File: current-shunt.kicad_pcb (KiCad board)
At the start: 4 copper layers, 130 x 50 mm, 187 parts, among them J1 Screw_Terminal_01x03, J2 Screw_Terminal_01x03, J3 Screw_Terminal_01x03, J4 Conn_01x02, J5 Conn_01x04, J6 Conn_01x04, U1 ADS1015IDGS, U2 INA219AxD, U3 INA219AxD, U4 INA219AxD, U5 MCP9804_MSOP, U6 M24C02-WMN, U7 TSR_1-2450, U8 ISO1541, U9 SRV05-4

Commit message: Add labels to board and update not available component
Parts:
- D15, D16, D19, D26, D27, D30, D35, D4, D5, D8: value P4SMAJ20CA -> SMAJ20CA
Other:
- board text added: "https://github.com/tdittr/tripple-current-shunt ${DATE} ${REV} CERN-OHL-P-2.0"
- board text removed: "https://github.com/tdittr/tripple-current-shunt CERN-OHL-P-2.0"
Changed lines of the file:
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@@
     )
   )
+  (property "DATE" "2022-10-28")
+  (property "REV" "rev1")
   (net 0 "")
   (net 1 "/shunt-a/IN+")
@@
     (descr "Diode SMA (DO-214AC)")
     (tags "Diode SMA (DO-214AC)")
-    (property "LCSC Part #" "C391567")
+    (property "LCSC Part #" "C309871")
     (property "Sheetfile" "File: shunt.kicad_sch")
     (property "Sheetname" "shunt-b")
@@
       (effects (font (size 1 1) (thickness 0.15)))
     )
-    (fp_text value "P4SMAJ20CA" (at 0 2.6 90) (layer "F.Fab")
+    (fp_text value "SMAJ20CA" (at 0 2.6 90) (layer "F.Fab")
       (effects (font (size 1 1) (thickness 0.15)))
     )
@@
     (descr "Diode SMA (DO-214AC)")
     (tags "Diode SMA (DO-214AC)")
-    (property "LCSC Part #" "C391567")
+    (property "LCSC Part #" "C309871")
     (property "Sheetfile" "File: shunt.kicad_sch")
     (property "Sheetname" "shunt-c")
@@
       (effects (font (size 1 1) (thickness 0.15)))
     )
-    (fp_text value "P4SMAJ20CA" (at 0 2.6 90) (layer "F.Fab")
+    (fp_text value "SMAJ20CA" (at 0 2.6 90) (layer "F.Fab")
       (effects (font (size 1 1) (thickness 0.15)))
     )
@@
     (descr "Diode SMA (DO-214AC)")
     (tags "Diode SMA (DO-214AC)")
-    (property "LCSC Part #" "C391567")
+    (property "LCSC Part #" "C309871")
     (property "Sheetfile" "File: shunt.kicad_sch")
     (property "Sheetname" "shunt-c")
@@
       (effects (font (size 1 1) (thickness 0.15)))
     )
-    (fp_text value "P4SMAJ20CA" (at 0 2.6 90) (layer "F.Fab")
+    (fp_text value "SMAJ20CA" (at 0 2.6 90) (layer "F.Fab")
       (effects (font (size 1 1) (thickness 0.15)))
     )
@@
     (descr "Diode SMA (DO-214AC)")
     (tags "Diode SMA (DO-214AC)")
-    (property "LCSC Part #" "C391567")
+    (property "LCSC Part #" "C309871")
     (property "Sheetfile" "File: shunt.kicad_sch")
     (property "Sheetname" "shunt-c")
@@
       (effects (font (size 1 1) (thickness 0.15)))
     )
-    (fp_text value "P4SMAJ20CA" (at 0 2.6 90) (layer "F.Fab")
+    (fp_text value "SMAJ20CA" (at 0 2.6 90) (layer "F.Fab")
       (effects (font (size 1 1) (thickness 0.15)))
     )
@@
     (descr "Diode SMA (DO-214AC)")
     (tags "Diode SMA (DO-214AC)")
-    (property "LCSC Part #" "C391567")
+    (property "LCSC Part #" "C309871")
     (property "Sheetfile" "File: shunt.kicad_sch")
     (property "Sheetname" "shunt-a")
@@
       (effects (font (size 1 1) (thickness 0.15)))
     )
-    (fp_text value "P4SMAJ20CA" (at 0 2.6 90) (layer "F.Fab")
+    (fp_text value "SMAJ20CA" (at 0 2.6 90) (layer "F.Fab")
       (effects (font (size 1 1) (thickness 0.15)))
     )
@@
     (descr "Diode SMA (DO-214AC)")
     (tags "Diode SMA (DO-214AC)")
-    (property "LCSC Part #" "C391567")
+    (property "LCSC Part #" "C309871")
     (property "Sheetfile" "File: shunt.kicad_sch")
     (property "Sheetname" "shunt-b")
@@
       (effects (font (size 1 1) (thickness 0.15)))
     )
-    (fp_text value "P4SMAJ20CA" (at 0 2.6 90) (layer "F.Fab")
+    (fp_text value "SMAJ20CA" (at 0 2.6 90) (layer "F.Fab")
       (effects (font (size 1 1) (thickness 0.15)))
     )
@@
     (descr "Diode SMA (DO-214AC)")
     (tags "Diode SMA (DO-214AC)")
-    (property "LCSC Part #" "C391567")
+    (property "LCSC Part #" "C309871")
     (property "Sheetfile" "File: shunt.kicad_sch")
     (property "Sheetname" "shunt-b")
@@
       (effects (font (size 1 1) (thickness 0.15)))
     )
-    (fp_text value "P4SMAJ20CA" (at 0 2.6 90) (layer "F.Fab")
+    (fp_text value "SMAJ20CA" (at 0 2.6 90) (layer "F.Fab")
       (effects (font (size 1 1) (thickness 0.15)))
     )
@@
     (descr "Diode SMA (DO-214AC)")
     (tags "Diode SMA (DO-214AC)")
-    (property "LCSC Part #" "C391567")
+    (property "LCSC Part #" "C309871")
     (property "Sheetfile" "File: shunt.kicad_sch")
     (property "Sheetname" "shunt-a")
@@
       (effects (font (size 1 1) (thickness 0.15)))
     )
-    (fp_text value "P4SMAJ20CA" (at 0 2.6 90) (layer "F.Fab")
+    (fp_text value "SMAJ20CA" (at 0 2.6 90) (layer "F.Fab")
       (effects (font (size 1 1) (thickness 0.15)))
     )
@@
     (descr "Diode SMA (DO-214AC)")
     (tags "Diode SMA (DO-214AC)")
-    (property "LCSC Part #" "C391567")
+    (property "LCSC Part #" "C309871")
     (property "Sheetfile" "File: shunt.kicad_sch")
     (property "Sheetname" "shunt-a")
@@
       (effects (font (size 1 1) (thickness 0.15)))
     )
-    (fp_text value "P4SMAJ20CA" (at 0 2.6 90) (layer "F.Fab")
+    (fp_text value "SMAJ20CA" (at 0 2.6 90) (layer "F.Fab")
       (effects (font (size 1 1) (thickness 0.15)))
     )
@@
     (descr "Diode SMA (DO-214AC)")
     (tags "Diode SMA (DO-214AC)")
-    (property "LCSC Part #" "C391567")
+    (property "LCSC Part #" "C309871")
     (property "Sheetfile" "File: current-shunt.kicad_sch")
     (property "Sheetname" "")
@@
       (effects (font (size 1 1) (thickness 0.15)))
     )
-    (fp_text value "P4SMAJ20CA" (at 0 2.6 90) (layer "F.Fab")
+    (fp_text value "SMAJ20CA" (at 0 2.6 90) (layer "F.Fab")
       (effects (font (size 1 1) (thickness 0.15)))
     )
@@
     (effects (font (size 1 1) (thickness 0.15)) (justify mirror))
   )
-  (gr_text "https://github.com/tdittr/tripple-current-shunt\nCERN-OHL-P-2.0" (at 154.305 60.325) (layer "B.SilkS")
-    (effects (font (size 1 1) (thickness 0.15)) (justify mirror))
+  (gr_text "https://github.com/tdittr/tripple-current-shunt\n${DATE} ${REV}\nCERN-OHL-P-2.0" (at 171.25 60.75) (layer "B.SilkS")
+    (effects (font (size 1 1) (thickness 0.15)) (justify left mirror))
   )
   (gr_text "I2C\nPullUp" (at 175.26 43.815) (layer "B.SilkS")

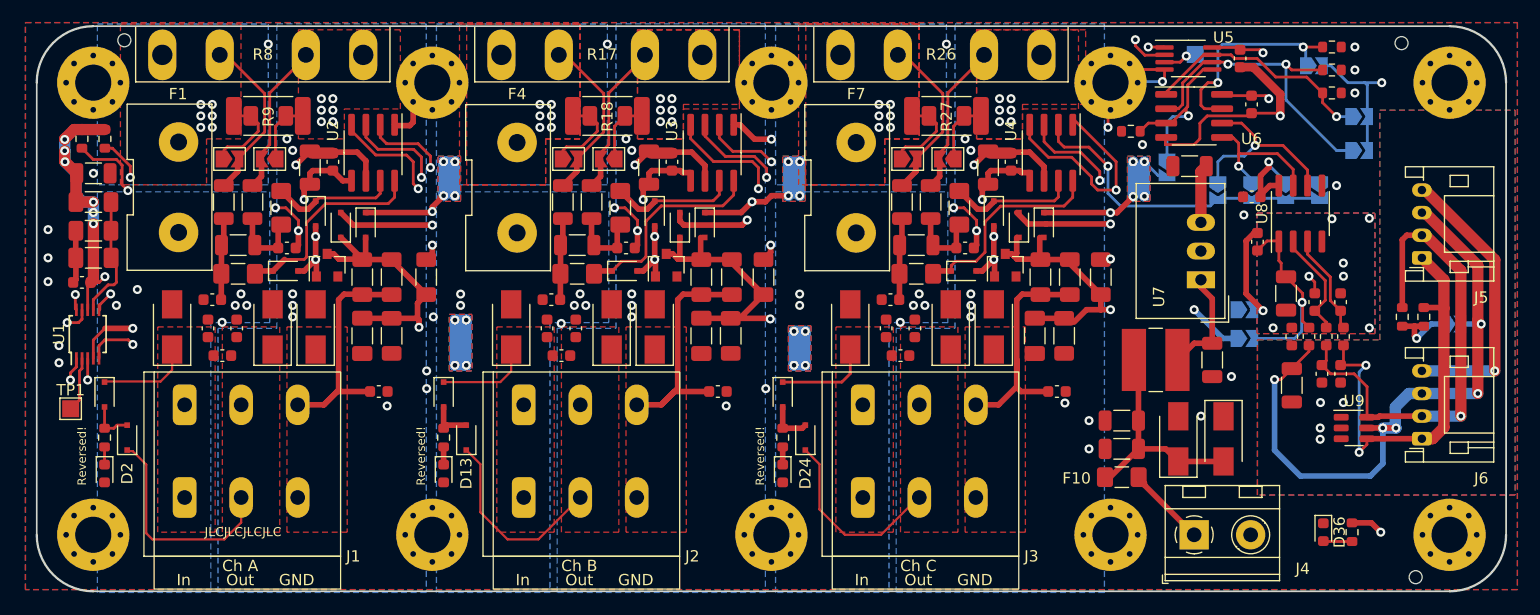
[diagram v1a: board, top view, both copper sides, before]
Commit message: Shrink board and reduce features to reduce price
* Shrink to 100mm x 50mm
* Remove voltage regulator and use Stemma Power instead
* Remove isolation (is easier to add outside when needed)
* Remove reverse indicators to save space
* Remove I2C pullups as they are no longer needed
* Fix A2 of EEPROM and Temperature sensor to 0 to save space
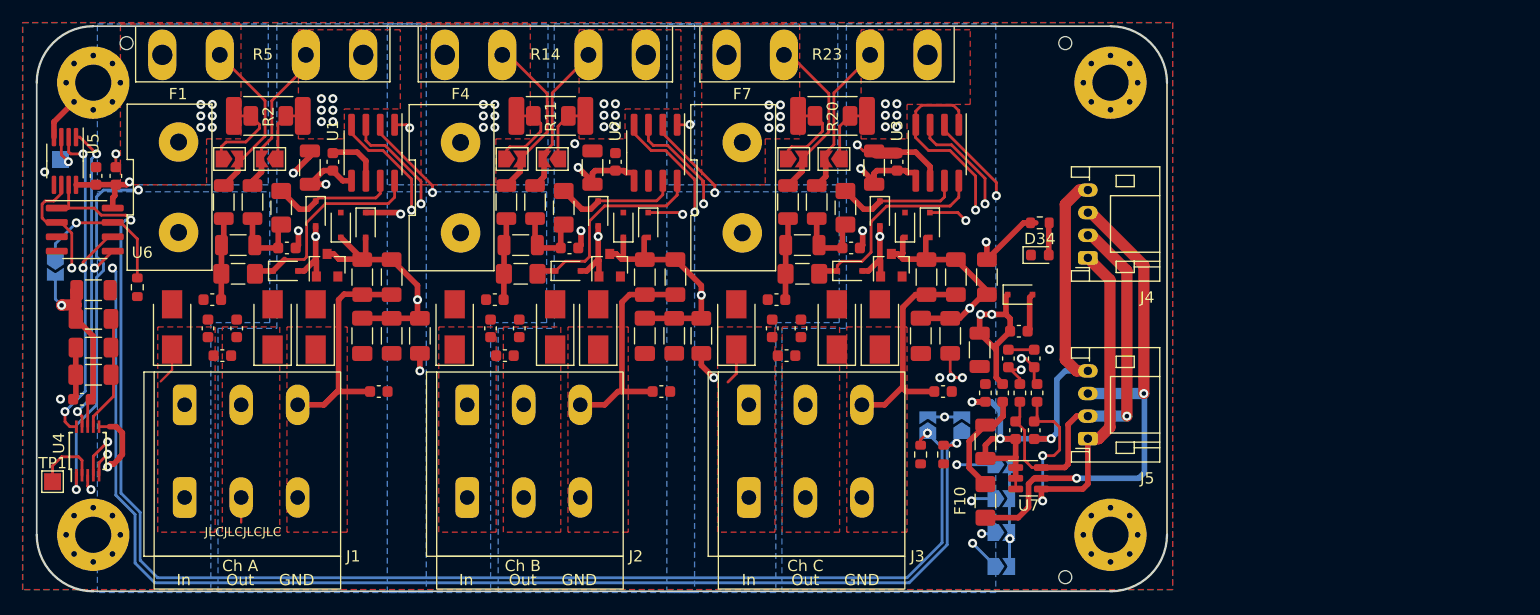
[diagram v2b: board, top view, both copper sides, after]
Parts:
- removed the C34 at (146.0, 54.9)
- removed the C35 at (146.0, 57.4)
- removed the C36 at (152.0, 32.4)
- removed the C37 at (154.0, 49.5)
- removed the C40 at (157.5, 35.1)
- removed D1, D12, D14, D23, D25, D3: PMEG4010BEA, Diode_SMD:D_SOD-323F
- removed D13, D2, D24, D36: LED, LED_SMD:LED_0603_1608Metric
- removed the H1 at (55.0, 25.0)
- removed the H2 at (55.0, 65.0)
- removed the H3 at (85.0, 25.0)
- removed the H4 at (85.0, 65.0)
- removed H5, H6: MountingHole_Pad, MountingHole:MountingHole_3.2mm_M3_Pad_Via
- removed the J4 at (152.4, 65.0)
- removed the JP14 at (156.8, 45.1)
- removed JP15, JP17: SolderJumper_2_Open, Jumper:SolderJumper-2_P1.3mm_Open_TrianglePad1.0x1.5mm
- removed the JP7 at (175.3, 46.4)
- removed L1: TCK-047, Inductor_SMD:L_TracoPower_TCK-047_5.2x5.8mm
- removed R1, R37, R38: 1K, Resistor_SMD:R_0603_1608Metric
- removed the R14 at (86.0, 56.4)
- removed the R23 at (116.0, 56.4)
- removed R32: 10K, Resistor_SMD:R_0603_1608Metric
- removed R36: 1K5, Resistor_SMD:R_0603_1608Metric
- removed the R4 at (56.0, 30.0)
- removed the R5 at (56.0, 56.4)
- removed the U7 at (153.0, 42.4)
- removed U8: ISO1541, Package_SO:SOIC-8_3.9x4.9mm_P1.27mm
- added R34: 1K5, Resistor_SMD:R_0603_1608Metric, F.Cu at (138.8, 37.4)
- D34: value M7 -> LED; footprint Diode_SMD:D_SMA -> LED_SMD:LED_0603_1608Metric
- D35: value SMAJ20CA -> PMEG4010BEA; footprint Diode_SMD:D_SMA -> Diode_SMD:D_SOD-323F
- moved JP14 112.8 mm to (51.6, 41.3), turned to -90 degrees
- moved R33 107.8 mm to (58.9, 43.1), turned to -90 degrees
- moved C34 101.7 mm to (55.2, 33.2), turned to 90 degrees
- moved TP2 100.8 mm to (52.1, 31.8)
- moved C35 100.7 mm to (57.0, 33.2), turned to 90 degrees
- moved U5 99.8 mm to (52.5, 31.9), turned to -90 degrees
- moved U6 98.7 mm to (54.2, 38.0)
- moved H1 90.0 mm to (55.0, 65.0)
- moved H3 90.0 mm to (55.0, 25.0)
- moved LOGO1 85.5 mm to (79.7, 64.0)
- moved R30 48.5 mm to (128.2, 57.9), turned to -90 degrees
- moved R31 48.4 mm to (130.2, 57.9), turned to -90 degrees
- moved JP11 46.9 mm to (128.8, 55.3), turned to 90 degrees
- moved JP12 42.7 mm to (131.8, 55.3), turned to 90 degrees
- moved JP4 38.4 mm to (135.3, 67.8), turned to 0 degrees
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- renumbered C10 to C1, C5 to C10, C20 to C11, C21 to C12, C14 to C13, C16 to C14, C18 to C15, C23 to C16, C22 to C17, C17 to C18, C11 to C2, C15 to C20, C30 to C21, C31 to C22, C24 to C23, C26 to C24, C28 to C25, C33 to C26, C32 to C27, C27 to C28, C4 to C3, C25 to C30, C3 to C31, C2 to C32, C1 to C33, C38 to C34, C39 to C35, C41 to C36, C42 to C37, C44 to C38, C46 to C39, C6 to C4, C43 to C40, C45 to C41, C47 to C42, C8 to C5, C13 to C6, C12 to C7, C7 to C8, D7 to D10, D9 to D11, D19 to D15, D15 to D16, D16 to D17, D22 to D18, D21 to D19, D17 to D20, D18 to D21, D20 to D22, D30 to D26, D26 to D27, D27 to D28, D33 to D29, D32 to D30, D28 to D31, D29 to D32, D31 to D33, D8 to D4, D4 to D5, D5 to D6, D11 to D7, D10 to D8, D6 to D9, FB2 to FB1, FB3 to FB2, FB4 to FB3, FB1 to FB4, H8 to H1, H9 to H2, H7 to H3, H10 to H4, J5 to J4, J6 to J5, JP11 to JP1, JP6 to JP10, JP8 to JP11, JP9 to JP12, JP10 to JP14, JP12 to JP2, JP13 to JP3, JP16 to JP4, JP1 to JP5, JP2 to JP6, JP3 to JP7, JP4 to JP8, JP5 to JP9, LOGO3 to LOGO2, LOGO2 to LOGO3, R18 to R11, R21 to R12, R19 to R13, R17 to R14, R22 to R17, R20 to R18, R9 to R2, R27 to R20, R29 to R21, R28 to R22, R26 to R23, R31 to R26, R30 to R27, R2 to R28, R3 to R29, R11 to R3, R35 to R30, R34 to R31, R10 to R4, R8 to R5, R13 to R8, R12 to R9, U2 to U1, U3 to U2, U4 to U3, U1 to U4, U9 to U7
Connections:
- C36 pad 1: Net-(C41-Pad1) -> +5V
- C36 pad 2: Net-(C41-Pad2) -> GND
- C37 pad 1: Net-(C41-Pad1) -> +5V
- C37 pad 2: Net-(C41-Pad2) -> GND
- C38 pad 1: Net-(C44-Pad1) -> /SDA
- C38 pad 2: Net-(C41-Pad2) -> GND
- C39 pad 1: Net-(C46-Pad1) -> /SCL
- C39 pad 2: Net-(C41-Pad2) -> GND
- C40 pad 1: /i2c-interface/Vcc_e -> Net-(C40-Pad1)
- D34 pad 1: Net-(C34-Pad1) -> GND
- D34 pad 2: GND -> Net-(D34-Pad2)
- D35 pad 1: GND -> +5V
- D35 pad 2: Net-(C34-Pad1) -> GND
- F10 pad 1: Net-(F10-Pad1) -> Net-(C40-Pad1)
- F10 pad 2: Net-(C34-Pad1) -> /i2c-interface/Vcc_e
- FB1 pad 1: Net-(C41-Pad1) -> +5V
- FB1 pad 2: /i2c-interface/Vcc_e -> Net-(C40-Pad1)
- FB2 pad 1: Net-(C44-Pad1) -> /SDA
- FB3 pad 1: Net-(C46-Pad1) -> /SCL
- FB4 pad 1: Net-(C41-Pad2) -> GND
- U5 pad 5: /temperature-sensor-eeprom/A2 -> GND
- U6 pad 3: /temperature-sensor-eeprom/A2 -> GND
- U7 pad 1: unconnected-(U9-Pad1) -> /i2c-interface/GND_e
- U7 pad 3: unconnected-(U9-Pad3) -> /i2c-interface/GND_e
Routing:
- net /temperature-sensor-eeprom/A0: track 20.7 -> 126.0 mm, vias 1 -> 2
- net /temperature-sensor-eeprom/A1: track 27.7 -> 128.5 mm, vias 2 -> 3
- net +5V: track 164.0 -> 85.9 mm, vias 43 -> 16
- net GND: track 128.9 -> 73.9 mm, vias 81 -> 19
- net /i2c-interface/GND_e: track 25.3 -> 50.9 mm, vias 5 -> 3
- net Net-(C34-Pad1): track 20.0 -> 0.00 mm
- net /gnd-level/A0: track 158.8 -> 177.1 mm, vias 4 -> 6
- net Net-(C41-Pad1): track 18.3 -> 0.00 mm, vias 1 -> 0
- net /shunt-a/IN-: track 25.9 -> 8.22 mm
- net /shunt-b/IN-: track 23.6 -> 6.18 mm
- net /shunt-c/IN-: track 23.0 -> 5.78 mm
- net /temperature-sensor-eeprom/A2: track 15.9 -> 0.00 mm, vias 1 -> 0
- net /i2c-interface/Vcc_e: track 58.9 -> 47.1 mm, vias 5 -> 2
- net Net-(C41-Pad2): track 10.8 -> 0.00 mm, vias 8 -> 0
- net Net-(C37-Pad1): track 9.72 -> 0.00 mm
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- removed copper zone on B.Cu, net +5V
- removed copper zone on F.Cu, net +5V
- removed copper zone on B.Cu, net /i2c-interface/GND_e
- removed copper zone on F.Cu, net /i2c-interface/GND_e
- removed copper zone on B.Cu, net Net-(C41-Pad2)
- removed copper zone on F.Cu, net Net-(C41-Pad2)
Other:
- board size 130 x 50 mm -> 100 x 50 mm
- board text added: "I2C Address Bits 1:0"
- board text removed: "Bits 1:0"
- board text removed: "I2C Address"
- board text removed: "I2C PullUp"
- board text removed: "Isolation Bridge"
- board text removed: "Reversed!"

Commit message: Improve I2C documentation
* Add note about Grove Connector quirk
* Add signal labels to board
* Add full list of I2C addresses
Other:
- board text added: "GND Vcc SDA SCL"
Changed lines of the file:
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@@
   (gr_line (start 150 25) (end 150 65) (layer "Edge.Cuts") (width 0.15))
   (gr_line (start 145 70) (end 55 70) (layer "Edge.Cuts") (width 0.15))
+  (gr_text "GND\nVcc\nSDA\nSCL" (at 147 53.5) (layer "B.SilkS")
+    (effects (font (size 1.5 1.5) (thickness 0.3)) (justify mirror))
+  )
   (gr_text "10" (at 130.339 64.8 90) (layer "B.SilkS")
     (effects (font (size 1 1) (thickness 0.15)) (justify mirror))
@@
     (effects (font (size 1 1) (thickness 0.15)) (justify mirror))
   )
+  (gr_text "GND\nVcc\nSDA\nSCL" (at 147 37.5) (layer "B.SilkS")
+    (effects (font (size 1.5 1.5) (thickness 0.3)) (justify mirror))
+  )
   (gr_text "https://github.com/tdittr/tripple-current-shunt\n${DATE} ${REV} CERN-OHL-P-2.0" (at 125 67) (layer "B.SilkS")

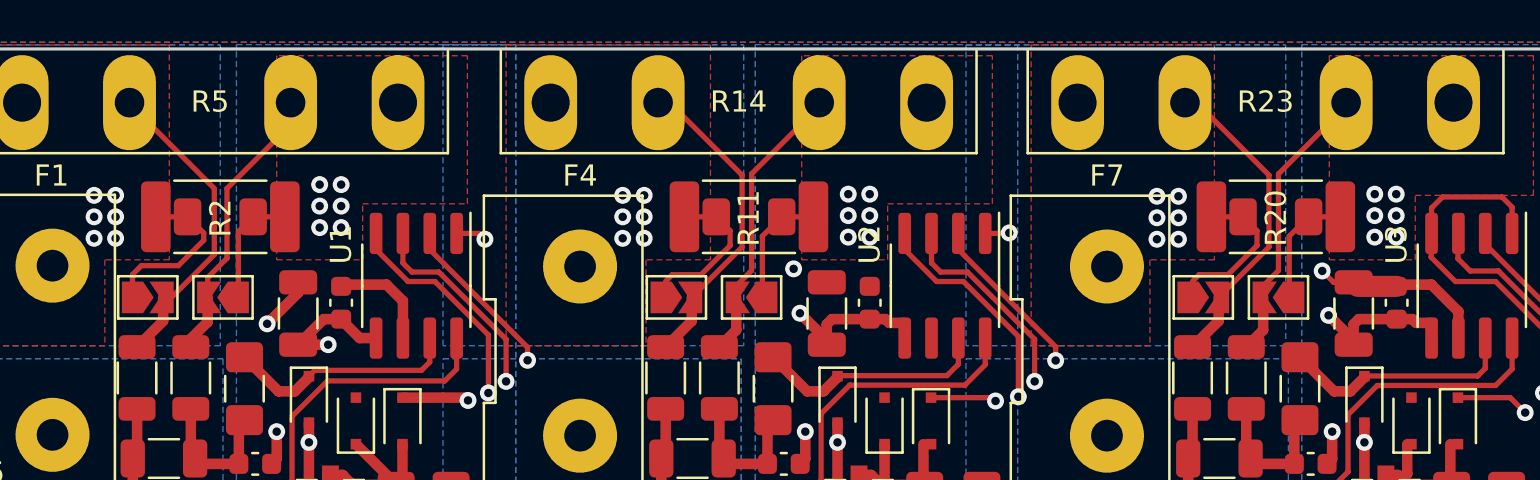
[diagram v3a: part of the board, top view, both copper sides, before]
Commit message: Switch shunt footprint
The 2816 footprint is big enough to also mount all the smaller
resistors down to 1206 and allows munting the bigger 2816
resistors.
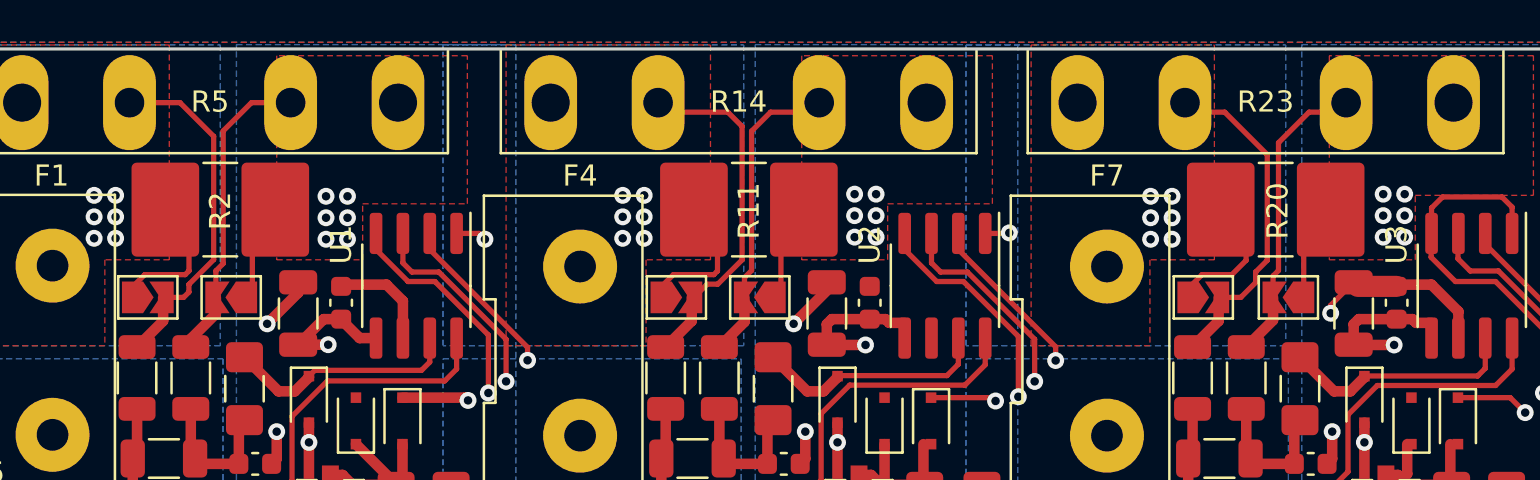
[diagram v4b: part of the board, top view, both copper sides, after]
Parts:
- R11, R2, R20: footprint Project_Footprints:R_Dual_2512_1206_Handsolder -> Resistor_SMD:R_2816_7142Metric_Pad3.20x4.45mm_HandSolder
- moved JP10 0.47 mm to (121.0, 31.8)
- moved JP6 0.39 mm to (71.0, 31.8)
- moved JP8 0.39 mm to (96.0, 31.8)
- moved R20 0.34 mm to (120.4, 27.6)
- moved R11 0.34 mm to (95.5, 27.6)
- moved R2 0.34 mm to (70.5, 27.6)
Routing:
- net GND: track 73.9 -> 76.7 mm
- net Net-(JP5-Pad2): track 15.0 -> 16.7 mm
- net Net-(JP7-Pad2): track 14.8 -> 16.5 mm
- net /shunt-a/IN+F: track 8.05 -> 6.84 mm
- net Net-(JP8-Pad2): track 13.2 -> 14.4 mm
- net /shunt-c/IN-: track 5.78 -> 4.68 mm
- net Net-(JP6-Pad2): track 13.5 -> 14.6 mm
- net Net-(JP9-Pad2): track 14.8 -> 15.9 mm
- net /shunt-b/IN-: track 6.18 -> 5.22 mm
- net /shunt-a/IN-: track 8.22 -> 7.33 mm
- net Net-(JP10-Pad2): track 13.2 -> 14.1 mm
